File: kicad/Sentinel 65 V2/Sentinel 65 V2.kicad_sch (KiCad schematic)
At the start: 158 parts, among them J1 SNES Controller, J11 Conn_01x02, J12 Conn_01x02, J13 LEFT, J14 RIGHT, J15 USB_C_Receptacle_PowerOnly_6P, J2 SNES Controller, J3 Conn_02x14_Odd_Even, J4 JTAG Header, J5 2x32 2.54mm Card Edge Connect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, J6 Internal Control Header (Opti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, J7 Conn_02x03_Odd_Even, J8 SD_Card, J9 SVGA Connector, SW1 SW_Push, SW2 SW_Push, U1 SST39LF040-55-4C-NHE-T, U10 WM8524CGEDT, U11 TLV9062xD, U12 LM1086IT-3.3, U13 MCP1316MT-33LE/OT, U2 W65C265S8PLG-8, U3 IS61WV5128EDBLL-10TLI, U4 ATF1502ASV-xAx44, U5 W25Q16JVSNIQ, U6 74CBTLV3126PW,118, U7 AP7361C-12E, U8 Si5351A, U9 ICE40UP5K-SG48ITR, Y1 25MHz

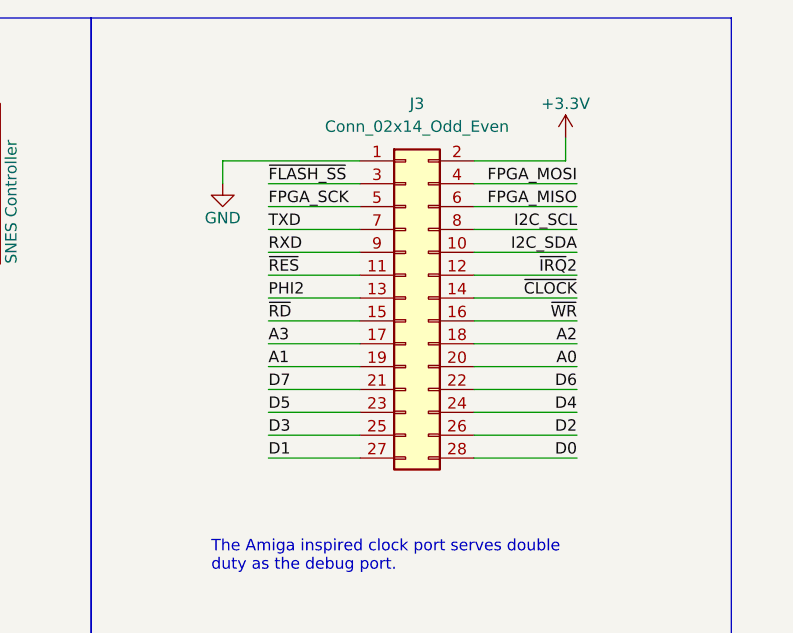
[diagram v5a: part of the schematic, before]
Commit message: Added FPGA pins CDONE and RESET to the clock port.
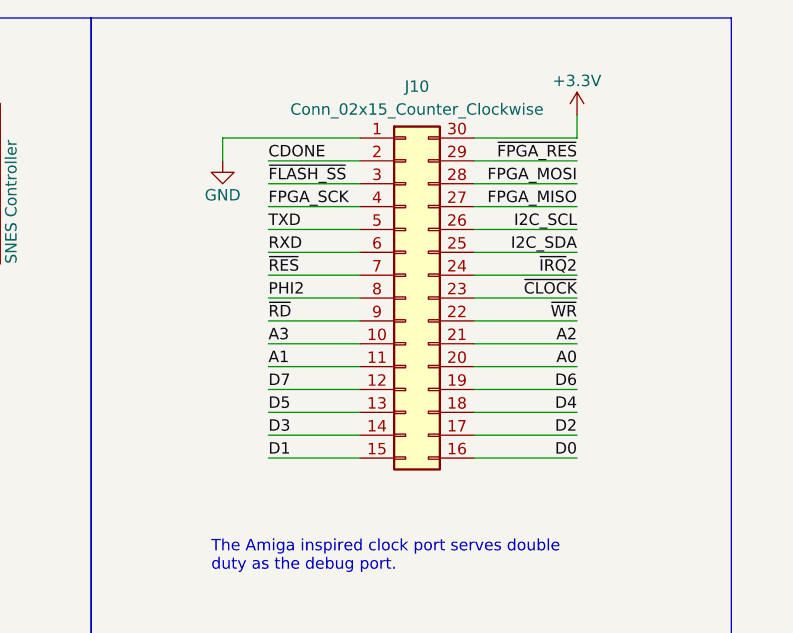
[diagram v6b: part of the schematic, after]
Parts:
- removed J3: Conn_02x14_Odd_Even, symbol Sentinel 65X:Conn_02x14_Odd_Even
- added J10: Conn_02x15_Counter_Clockwise, symbol Connector_Generic:Conn_02x15_Counter_Clockwise
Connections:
- net +3.3V: now also J10.30 (Pin_30)
- net A0: now also J10.20 (Pin_20)
- net A1: now also J10.11 (Pin_11)
- net A2: now also J10.21 (Pin_21)
- net A3: now also J10.10 (Pin_10)
- net CDONE: now also J10.2 (Pin_2)
- net D0: now also J10.16 (Pin_16)
- net D1: now also J10.15 (Pin_15)
- net D2: now also J10.17 (Pin_17)
- net D3: now also J10.14 (Pin_14)
- net D4: now also J10.18 (Pin_18)
- net D5: now also J10.13 (Pin_13)
- net D6: now also J10.19 (Pin_19)
- net D7: now also J10.12 (Pin_12)
- net FPGA_MISO: now also J10.27 (Pin_27)
- net FPGA_MOSI: now also J10.28 (Pin_28)
- net FPGA_SCK: now also J10.4 (Pin_4)
- net GND: now also J10.1 (Pin_1)
- net I2C_SCL: now also J10.26 (Pin_26)
- net I2C_SDA: now also J10.25 (Pin_25)
- net PHI2: now also J10.8 (Pin_8)
- net RXD: now also J10.6 (Pin_6)
- net TXD: now also J10.5 (Pin_5)
- net ~{CLOCK}: now also J10.23 (Pin_23)
- net ~{FLASH_SS}: now also J10.3 (Pin_3)
- net ~{FPGA_RES}: now also J10.29 (Pin_29)
- net ~{IRQ}2: now also J10.24 (Pin_24)
- net ~{RD}: now also J10.9 (Pin_9)
- net ~{RES}: now also J10.7 (Pin_7)
- net ~{WR}: now also J10.22 (Pin_22)
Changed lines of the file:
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@@
     (stroke (width 0) (type default))
   )
+  (wire (pts (xy 485.775 28.575) (xy 495.935 28.575))
+    (stroke (width 0) (type default))
+  )
   (wire (pts (xy 351.79 36.83) (xy 363.22 36.83))
     (stroke (width 0) (type default))
@@
     (stroke (width 0) (type default))
   )
+  (wire (pts (xy 520.065 23.495) (xy 520.065 26.035))
+    (stroke (width 0) (type default))
+  )
   (wire (pts (xy 497.84 216.535) (xy 497.84 219.075))
     (stroke (width 0) (type default))
@@
     (stroke (width 0) (type default))
   )
+  (wire (pts (xy 480.695 26.035) (xy 480.695 28.575))
+    (stroke (width 0) (type default))
+  )
   (wire (pts (xy 417.83 239.395) (xy 420.37 239.395))
     (stroke (width 0) (type default))
@@
     (stroke (width 0) (type default))
   )
+  (wire (pts (xy 520.065 28.575) (xy 508.635 28.575))
+    (stroke (width 0) (type default))
+  )
   (wire (pts (xy 476.885 293.37) (xy 476.885 294.005))
     (stroke (width 0) (type default))
@@
     (stroke (width 0) (type default))
   )
-  (wire (pts (xy 480.695 28.575) (xy 495.935 28.575))
-    (stroke (width 0) (type default))
-  )
   (wire (pts (xy 254 50.8) (xy 243.84 50.8))
     (stroke (width 0) (type default))
@@
     (stroke (width 0) (type default))
   )
+  (wire (pts (xy 508.635 26.035) (xy 520.065 26.035))
+    (stroke (width 0) (type default))
+  )
   (wire (pts (xy 254 195.58) (xy 264.16 195.58))
     (stroke (width 0) (type default))
@@
     (stroke (width 0) (type default))
   )
-  (wire (pts (xy 518.795 26.035) (xy 518.795 28.575))
-    (stroke (width 0) (type default))
-  )
   (wire (pts (xy 472.44 293.37) (xy 472.44 294.005))
     (stroke (width 0) (type default))
@@
     (stroke (width 0) (type default))
   )
-  (wire (pts (xy 480.695 28.575) (xy 480.695 31.115))
-    (stroke (width 0) (type default))
-  )
   (wire (pts (xy 130.81 367.665) (xy 142.24 367.665))
     (stroke (width 0) (type default))
@@
     (stroke (width 0) (type default))
   )
-  (wire (pts (xy 508.635 28.575) (xy 518.795 28.575))
-    (stroke (width 0) (type default))
-  )
   (wire (pts (xy 44.45 209.55) (xy 44.45 217.17))
     (stroke (width 0) (type default))
@@
     (stroke (width 0) (type default))
   )
+  (wire (pts (xy 480.695 26.035) (xy 495.935 26.035))
+    (stroke (width 0) (type default))
+  )
   (wire (pts (xy 448.31 203.835) (xy 449.58 203.835))
     (stroke (width 0) (type default))
@@
     (effects (font (size 1.27 1.27)) (justify right bottom))
   )
+  (label "CDONE" (at 485.775 28.575 0) (fields_autoplaced)
+    (effects (font (size 1.27 1.27)) (justify left bottom))
+  )
   (label "A18" (at 351.79 49.53 0) (fields_autoplaced)
     (effects (font (size 1.27 1.27)) (justify left bottom))
@@
     (effects (font (size 1.27 1.27)) (justify left bottom))
   )
+  (label "~{FPGA_RES}" (at 520.065 28.575 180) (fields_autoplaced)
+    (effects (font (size 1.27 1.27)) (justify right bottom))
+  )
   (label "~{IRQ}3" (at 351.79 80.01 0) (fields_autoplaced)
     (effects (font (size 1.27 1.27)) (justify left bottom))
@@
     )
   )
-  (symbol (lib_id "Sentinel 65X:Conn_02x14_Odd_Even") (at 501.015 43.815 0) (unit 1)
-    (in_bom yes) (on_board yes) (dnp no) (fields_autoplaced)
-    (property "Reference" "J3" (at 502.285 22.225 0)
-      (effects (font (size 1.27 1.27)))
-    )
-    (property "Value" "Conn_02x14_Odd_Even" (at 502.285 24.765 0)
-      (effects (font (size 1.27 1.27)))
-    )
-    (property "Footprint" "" (at 501.015 43.815 0)
-      (effects (font (size 1.27 1.27)) hide)
-    )
-    (property "Datasheet" "~" (at 501.015 43.815 0)
-      (effects (font (size 1.27 1.27)) hide)
-    )
-    (pin "1")
-    (pin "10")
-    (pin "11")
-    (pin "12")
-    (pin "13")
-    (pin "14")
-    (pin "15")
-    (pin "16")
-    (pin "17")
-    (pin "18")
-    (pin "19")
-    (pin "2")
-    (pin "20")
-    (pin "21")
-    (pin "22")
-    (pin "23")
-    (pin "24")
-    (pin "25")
-    (pin "26")
-    (pin "27")
-    (pin "28")
-    (pin "3")
-    (pin "4")
-    (pin "5")
-    (pin "6")
-    (pin "7")
-    (pin "8")
-    (pin "9")
-    (instances
-      (project "Sentinel 65 V2"
-        (path "/a2a8ce47-493a-4b72-bd2b-495163d6beb9"
-          (reference "J3") (unit 1)
-        )
-      )
-    )
-  )
   (symbol (lib_id "Sentinel 65X:Si5351A") (at 154.94 147.955 0) (unit 1)
     (in_bom yes) (on_board yes) (dnp no)
@@
     )
   )
+  (symbol (lib_id "Connector_Generic:Conn_02x15_Counter_Clockwise") (at 501.015 43.815 0) (unit 1)
+    (in_bom yes) (on_board yes) (dnp no) (fields_autoplaced)
+    (property "Reference" "J10" (at 502.285 20.32 0)
+      (effects (font (size 1.27 1.27)))
+    )
+    (property "Value" "Conn_02x15_Counter_Clockwise" (at 502.285 22.86 0)
+      (effects (font (size 1.27 1.27)))
+    )
+    (property "Footprint" "" (at 501.015 43.815 0)
+      (effects (font (size 1.27 1.27)) hide)
+    )
+    (property "Datasheet" "~" (at 501.015 43.815 0)
+      (effects (font (size 1.27 1.27)) hide)
+    )
+    (pin "1")
+    (pin "10")
+    (pin "11")
+    (pin "12")
+    (pin "13")
+    (pin "14")
+    (pin "15")
+    (pin "16")
+    (pin "17")
+    (pin "18")
+    (pin "19")
+    (pin "2")
+    (pin "20")
+    (pin "21")
+    (pin "22")
+    (pin "23")
+    (pin "24")
+    (pin "25")
+    (pin "26")
+    (pin "27")
+    (pin "28")
+    (pin "29")
+    (pin "3")
+    (pin "30")
+    (pin "4")
+    (pin "5")
+    (pin "6")
+    (pin "7")
+    (pin "8")
+    (pin "9")
+    (instances
+      (project "Sentinel 65 V2"
+        (path "/a2a8ce47-493a-4b72-bd2b-495163d6beb9"
+          (reference "J10") (unit 1)
+        )
+      )
+    )
+  )
   (symbol (lib_id "Sentinel 65X:R") (at 483.235 349.885 270) (mirror x) (unit 1)
     (in_bom yes) (on_board yes) (dnp no)
@@
     )
   )
-  (symbol (lib_id "power:GND") (at 480.695 31.115 0) (unit 1)
-    (in_bom yes) (on_board yes) (dnp no)
-    (property "Reference" "#PWR023" (at 480.695 37.465 0)
-      (effects (font (size 1.27 1.27)) hide)
-    )
-    (property "Value" "GND" (at 480.695 34.925 0)
-      (effects (font (size 1.27 1.27)))
-    )
-    (property "Footprint" "" (at 480.695 31.115 0)
-      (effects (font (size 1.27 1.27)) hide)
-    )
-    (property "Datasheet" "" (at 480.695 31.115 0)
-      (effects (font (size 1.27 1.27)) hide)
-    )
-    (pin "1")
-    (instances
-      (project "Sentinel 65 V2"
-        (path "/a2a8ce47-493a-4b72-bd2b-495163d6beb9"
-          (reference "#PWR023") (unit 1)
-        )
-      )
-    )
-  )
   (symbol (lib_id "Sentinel 65X:C") (at 149.225 139.065 0) (unit 1)
     (in_bom yes) (on_board yes) (dnp no) (fields_autoplaced)
@@
     )
   )
-  (symbol (lib_id "power:+3.3V") (at 518.795 26.035 0) (unit 1)
-    (in_bom yes) (on_board yes) (dnp no)
-    (property "Reference" "#PWR014" (at 518.795 29.845 0)
-      (effects (font (size 1.27 1.27)) hide)
-    )
-    (property "Value" "+3.3V" (at 518.795 22.225 0)
-      (effects (font (size 1.27 1.27)))
-    )
-    (property "Footprint" "" (at 518.795 26.035 0)
-      (effects (font (size 1.27 1.27)) hide)
-    )
-    (property "Datasheet" "" (at 518.795 26.035 0)
-      (effects (font (size 1.27 1.27)) hide)
-    )
-    (pin "1")
-    (instances
-      (project "Sentinel 65 V2"
-        (path "/a2a8ce47-493a-4b72-bd2b-495163d6beb9"
-          (reference "#PWR014") (unit 1)
-        )
-      )
-    )
-  )
   (symbol (lib_id "Sentinel 65X:R") (at 478.79 197.485 0) (mirror x) (unit 1)
     (in_bom yes) (on_board yes) (dnp no)
@@
     )
   )
+  (symbol (lib_id "power:+3.3V") (at 520.065 23.495 0) (unit 1)
+    (in_bom yes) (on_board yes) (dnp no)
+    (property "Reference" "#PWR014" (at 520.065 27.305 0)
+      (effects (font (size 1.27 1.27)) hide)
+    )
+    (property "Value" "+3.3V" (at 520.065 19.685 0)
+      (effects (font (size 1.27 1.27)))
+    )
+    (property "Footprint" "" (at 520.065 23.495 0)
+      (effects (font (size 1.27 1.27)) hide)
+    )
+    (property "Datasheet" "" (at 520.065 23.495 0)
+      (effects (font (size 1.27 1.27)) hide)
+    )
+    (pin "1")
+    (instances
+      (project "Sentinel 65 V2"
+        (path "/a2a8ce47-493a-4b72-bd2b-495163d6beb9"
+          (reference "#PWR014") (unit 1)
+        )
+      )
+    )
+  )
   (symbol (lib_id "power:+3.3V") (at 328.93 129.54 0) (unit 1)
     (in_bom yes) (on_board yes) (dnp no)
@@
         )
       )
+    )
+  )
+  (symbol (lib_id "power:GND") (at 480.695 28.575 0) (unit 1)
+    (in_bom yes) (on_board yes) (dnp no)
+    (property "Reference" "#PWR023" (at 480.695 34.925 0)
+      (effects (font (size 1.27 1.27)) hide)
+    )
+    (property "Value" "GND" (at 480.695 32.385 0)
+      (effects (font (size 1.27 1.27)))
+    )
+    (property "Footprint" "" (at 480.695 28.575 0)
+      (effects (font (size 1.27 1.27)) hide)
+    )
+    (property "Datasheet" "" (at 480.695 28.575 0)
+      (effects (font (size 1.27 1.27)) hide)
+    )
+    (pin "1")
+    (instances
+      (project "Sentinel 65 V2"
+        (path "/a2a8ce47-493a-4b72-bd2b-495163d6beb9"
+          (reference "#PWR023") (unit 1)
+        )
+      )
